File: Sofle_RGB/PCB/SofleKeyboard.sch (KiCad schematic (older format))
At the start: 95 parts, among them J1 LED, J2 4PIN, J3 OLED, J4 key leds, J5 backlight sel, J6 indicator bypass, P1 i2c_pin, P2 i2c_pin, SW1 SW_PUSH-MX_W_LED, SW10 SW_PUSH-MX_W_LED, SW11 SW_PUSH-MX_W_LED, SW12 SW_PUSH-MX_W_LED, SW13 SW_PUSH-MX_W_LED, SW14 SW_PUSH-MX_W_LED, SW15 SW_PUSH-MX_W_LED, SW16 SW_PUSH-MX_W_LED, SW17 SW_PUSH-MX_W_LED, SW18 SW_PUSH-MX_W_LED, SW19 SW_PUSH-MX_W_LED, SW2 SW_PUSH-MX_W_LED, SW20 SW_PUSH-MX_W_LED, SW21 SW_PUSH-MX_W_LED, SW22 SW_PUSH-MX_W_LED, SW23 SW_PUSH-MX_W_LED, SW24 SW_PUSH-MX_W_LED, SW25 Rotary_Encoder_Switch, SW26 SW_PUSH-MX_W_LED, SW27 SW_PUSH-MX_W_LED, SW28 SW_PUSH-MX_W_LED, SW29 SW_PUSH-MX_W_LED, SW3 SW_PUSH-MX_W_LED, SW30 SW_PUSH-MX_W_LED, SW4 SW_PUSH-MX_W_LED, SW5 SW_PUSH-MX_W_LED, SW6 SW_PUSH-MX_W_LED, SW7 SW_PUSH-MX_W_LED, SW8 SW_PUSH-MX_W_LED, SW9 SW_PUSH-MX_W_LED, U1 ProMicro

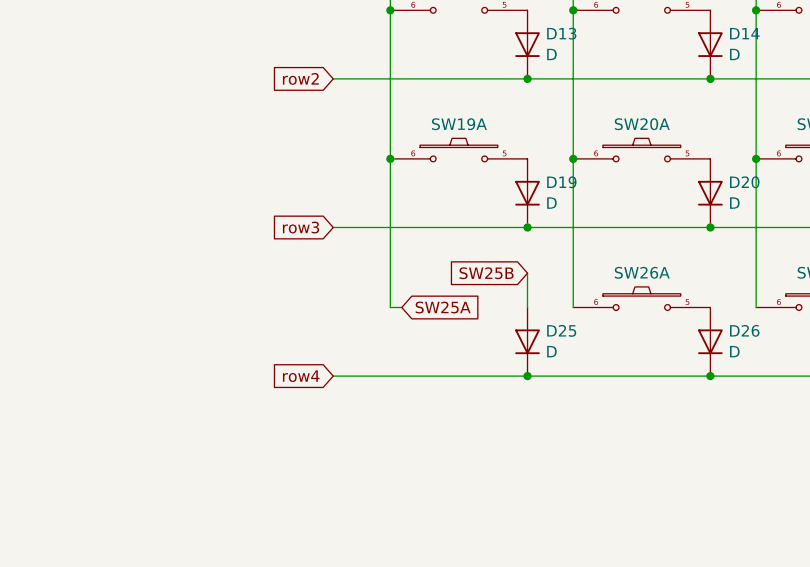
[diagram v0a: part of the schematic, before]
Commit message: Added SW31 into the place where the encoder is located.
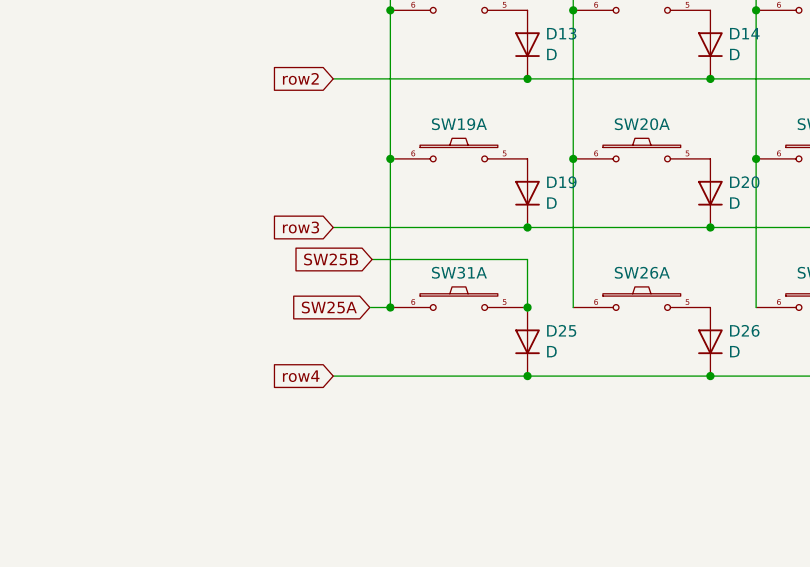
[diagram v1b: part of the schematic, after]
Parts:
- added SW31: SW_PUSH-MX_W_LED, footprints:cherry_mx, symbol SofleKeyboard:SW_PUSH-MX_W_LED
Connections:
- net SW25A: now also SW31.6
- net SW25B: now also SW31.5
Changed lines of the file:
@@
 Wire Wire Line
 	2850 6250 3150 6250
-Text GLabel 6350 6050 2    50   Input ~ 0
+Text GLabel 6210 6050 0    50   Input ~ 0
 SW25A
-Text GLabel 6900 5900 0    50   Input ~ 0
+Text GLabel 6220 5840 0    50   Input ~ 0
 SW25B
-Wire Wire Line
-	6900 5900 6900 6050
-Wire Wire Line
-	6300 6050 6350 6050
 Text GLabel 2400 1250 2    50   Input ~ 0
 ENCA
@@
 Wire Wire Line
 	4950 2400 4950 2700
+Wire Wire Line
+	6300 6050 6210 6050
+Connection ~ 6300 6050
+Wire Wire Line
+	6220 5840 6900 5840
+Wire Wire Line
+	6900 5840 6900 6050
+Connection ~ 6900 6050
+$Comp
+L SofleKeyboard:SW_PUSH-MX_W_LED SW31
+U 1 1 61E30679
+P 6600 6050
+F 0 "SW31" H 6600 6200 50  0000 C CNN
+F 1 "SW_PUSH-MX_W_LED" H 6600 5950 50  0001 C CNN
+F 2 "footprints:cherry_mx" H 6600 6050 50  0001 C CNN
+F 3 "" H 6600 6050 50  0000 C CNN
+	1    6600 6050
+	1    0    0    -1
+$EndComp
 $EndSCHEMATC
